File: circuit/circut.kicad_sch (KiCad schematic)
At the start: 6 parts, among them J1 ESP321, J3 Conn_02x04_Top_Bottom

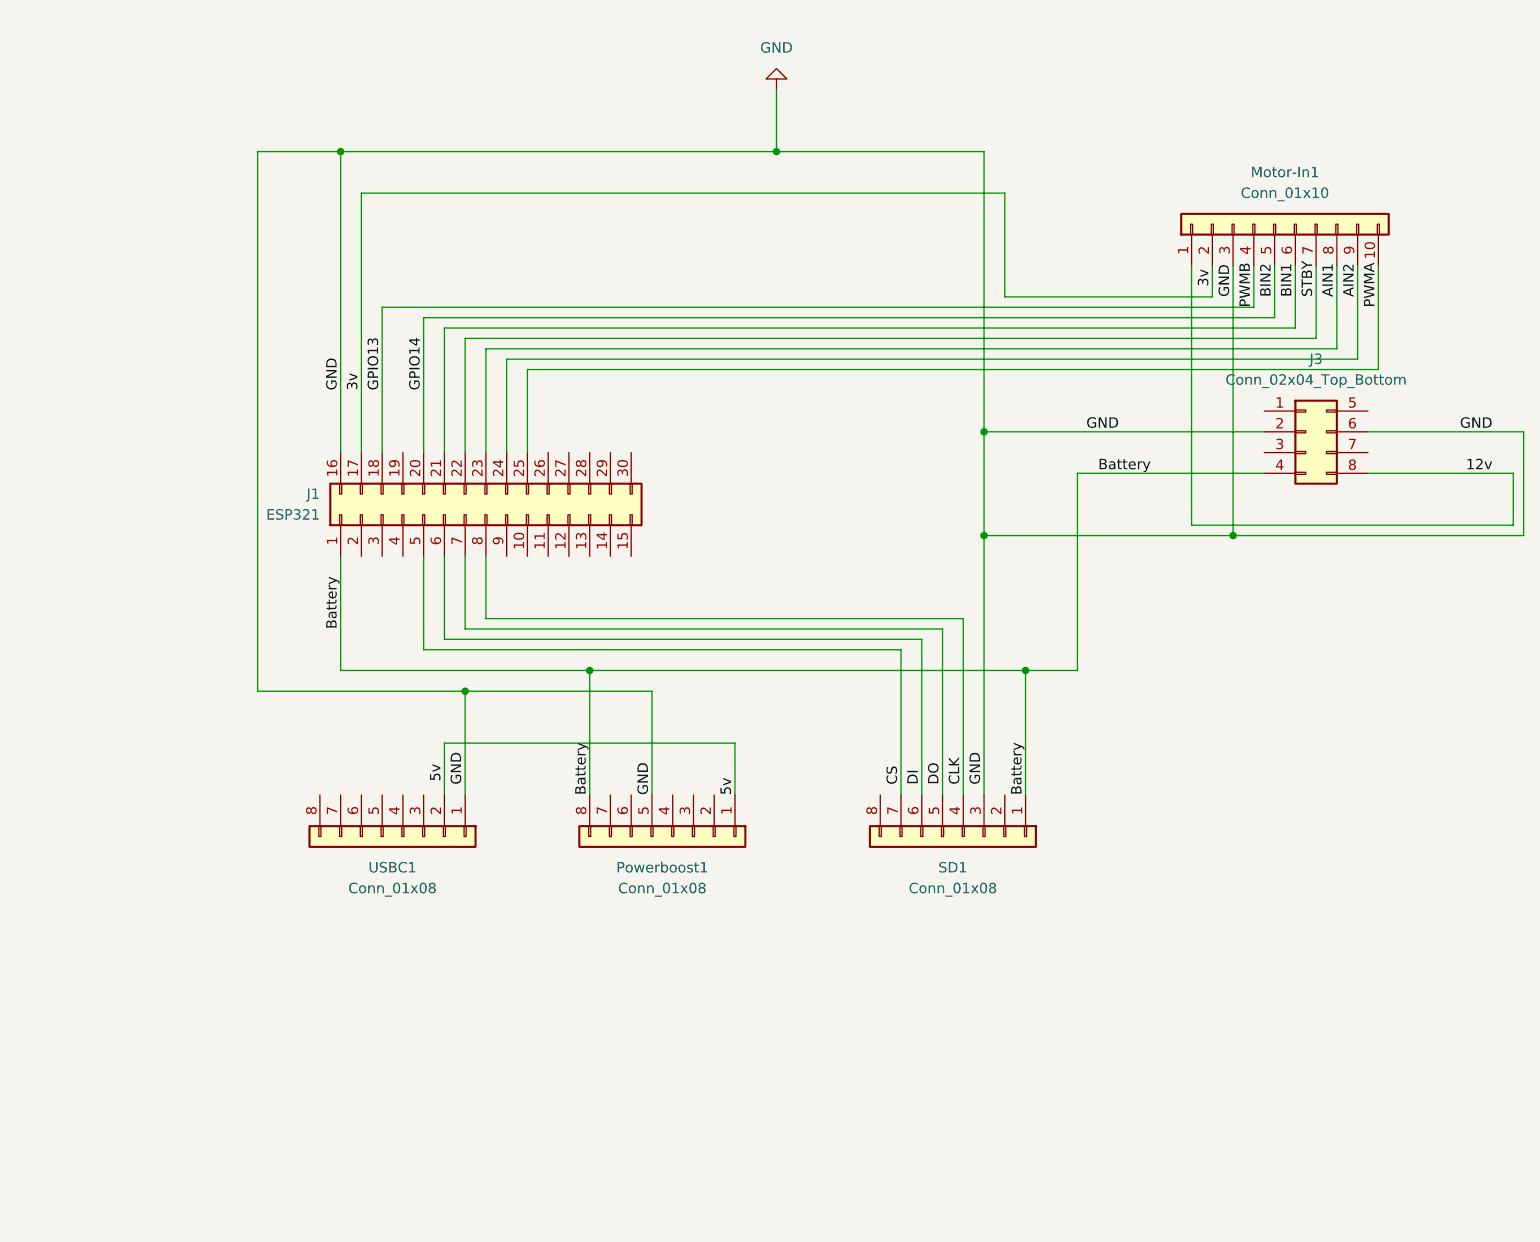
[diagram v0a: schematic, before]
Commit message: updating carrier board design
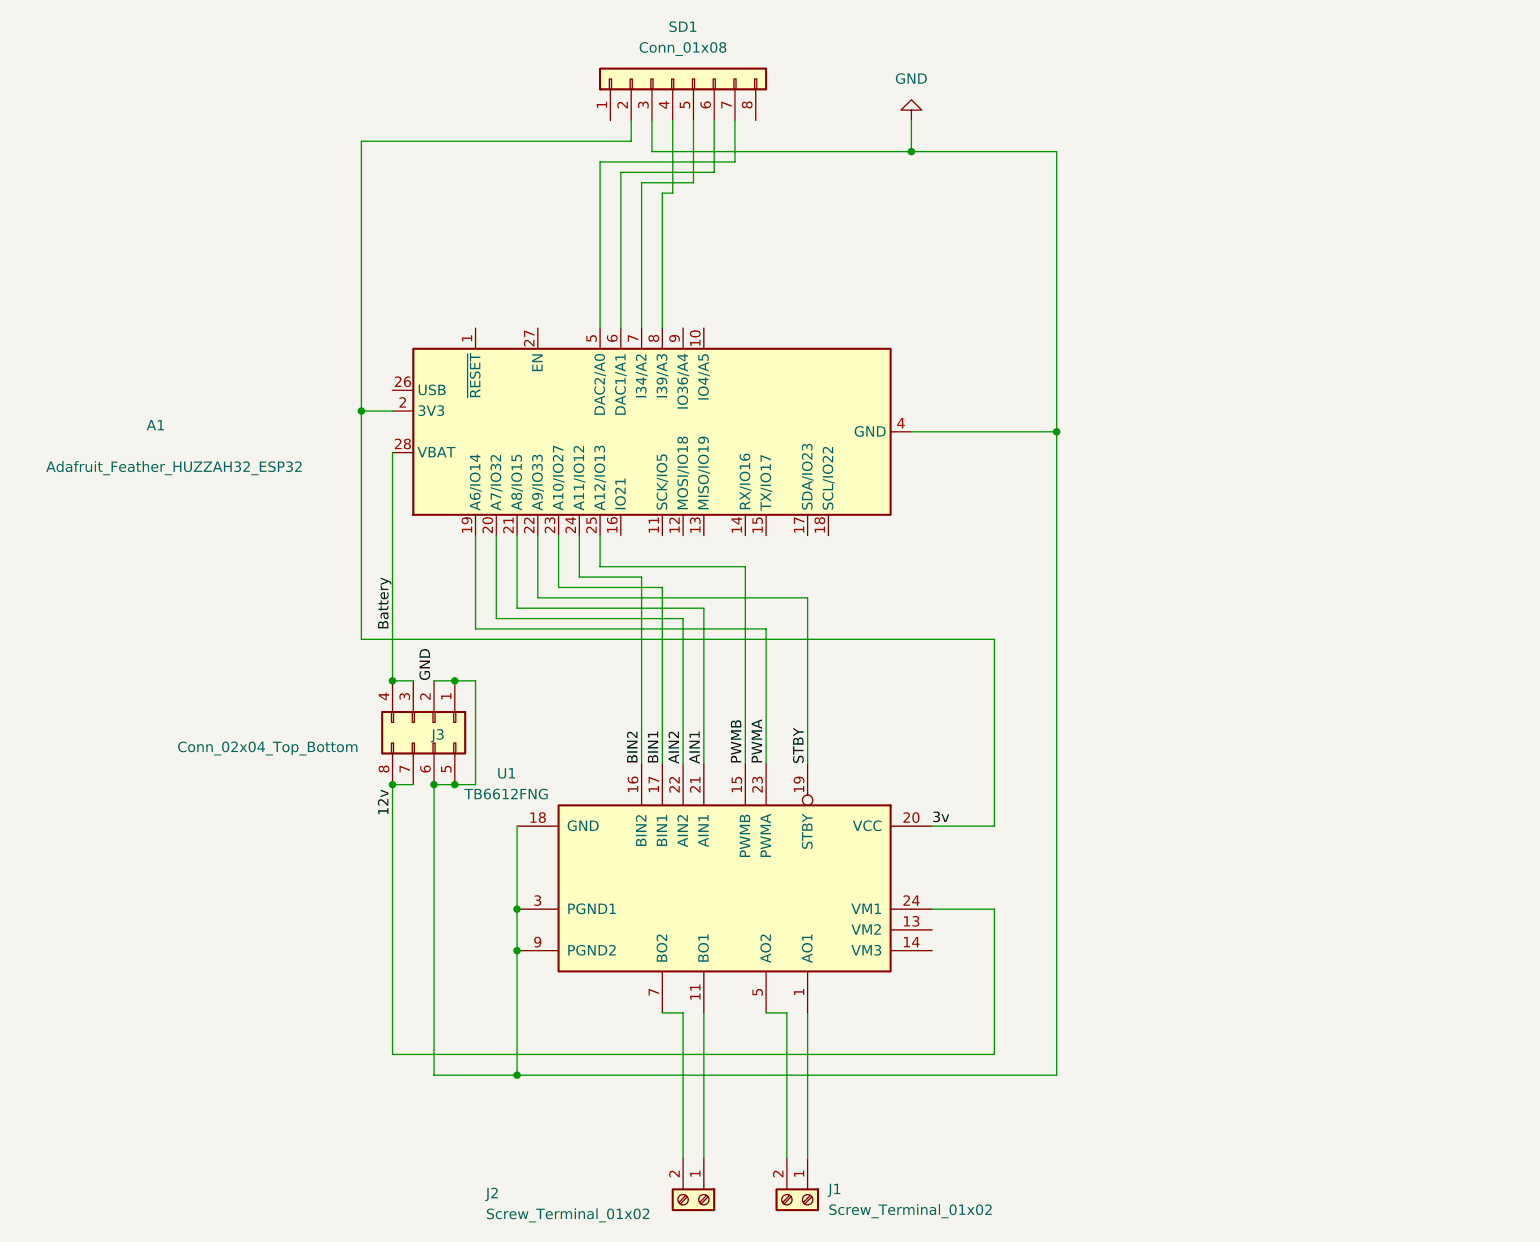
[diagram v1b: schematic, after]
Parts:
- removed J1: ESP321, Library:Adafruit_Huzzah32_breakout, symbol Connector_Generic:Conn_02x15_Top_Bottom
- removed Motor-In1: Conn_01x10, Library:Adafruit TB6612, symbol Connector_Generic:Conn_01x10
- removed Powerboost1: Conn_01x08, Library:Adafruit Powerboost 1000, symbol Connector_Generic:Conn_01x08
- removed USBC1: Conn_01x08, Library:Adafruit USB-C Breakout, symbol Connector_Generic:Conn_01x08
- added A1: Adafruit_Feather_HUZZAH32_ESP32, Module:Adafruit_Feather_WithMountingHoles, symbol MCU_Module:Adafruit_Feather_HUZZAH32_ESP32
- added J1, J2: Screw_Terminal_01x02, TerminalBlock_CUI:TerminalBlock_CUI_TB007-508-02_1x02_P5.08mm_Horizontal, symbol Connector:Screw_Terminal_01x02
- added U1: TB6612FNG, Library:Adafruit TB6612, symbol Driver_Motor:TB6612FNG
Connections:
- net 12v: now also J3.7 (Pin_7), U1.24 (VM1)
- net 3v: now also SD1.2 (Pin_2), A1.2 (3V3), U1.20 (VCC)
- net AIN1: now also A1.21 (A8/IO15), U1.21 (AIN1)
- net AIN2: now also A1.20 (A7/IO32), U1.22 (AIN2)
- net BIN1: now also A1.23 (A10/IO27), U1.17 (BIN1)
- net BIN2: now also A1.24 (A11/IO12), U1.16 (BIN2)
- net Battery: now also J3.3 (Pin_3), A1.28 (VBAT); no longer SD1.1 (Pin_1)
- net GND: now also J3.1 (Pin_1), J3.5 (Pin_5), A1.4 (GND), U1.10 (PGND2), U1.18 (GND), U1.3 (PGND1), U1.4 (PGND1), U1.9 (PGND2)
- net PWMA: now also A1.19 (A6/IO14), U1.23 (PWMA)
- net STBY: now also A1.22 (A9/IO33), U1.19 (STBY)
- net CLK: no longer names the net of SD1.4 (Pin_4)
- net CLK: now also A1.8 (I39/A3)
- net CS: no longer names the net of SD1.7 (Pin_7)
- net CS: now also A1.5 (DAC2/A0)
- net DI: no longer names the net of SD1.6 (Pin_6)
- net DI: now also A1.6 (DAC1/A1)
- net DO: no longer names the net of SD1.5 (Pin_5)
- net DO: now also A1.7 (I34/A2)
- new net: J2.1 (Pin_1), U1.11 (BO1), U1.12 (BO1)
- new net: J2.2 (Pin_2), U1.7 (BO2), U1.8 (BO2)
- new net: J1.1 (Pin_1), U1.1 (AO1), U1.2 (AO1)
- new net: J1.2 (Pin_2), U1.5 (AO2), U1.6 (AO2)
- new net PWMB: A1.25 (A12/IO13), U1.15 (PWMB)
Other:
- moved on the sheet: J3, SD1
